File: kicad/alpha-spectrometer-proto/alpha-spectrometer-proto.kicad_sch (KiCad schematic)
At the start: 78 parts, among them J1 USB_B_Micro, J13 Anode, J14 Catode, J19 Conn, J2 Conn_01x01_Female, J20 Conn_01x01_Female, J21 Conn_01x01_Female, J22 Conn_01x01_Female, J3 Conn_01x01_Female, J4 BAT+, J5 BAT-, Q1 IRLML5203, SW1 SW_Push_SPDT, U1 MAX4477, U2 LM2733XMF, U3 MCP73831, U5 LMV7239, U6 MCP1700x, U7 LT3045xMSE, Y1 16

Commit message: удалено:       kicad/alpha-spectrometer-proto/alpha-spectrometer-proto-backups/alpha-spectrometer-proto-2024-11-04_113452.zip 	изменено:      kicad/alpha-spectrometer-proto/alpha-spectrometer-proto.kicad_pcb 	изменено:      kicad/alpha-spectrometer-proto/alpha-spectrometer-proto.kicad_prl 	изменено:      kicad/alpha-spectrometer-proto/alpha-spectrometer-proto.kicad_sch
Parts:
- L1: footprint Inductor_SMD:L_1206_3216Metric -> Inductor_SMD:L_1206_3216Metric_Pad1.42x1.75mm_HandSolder
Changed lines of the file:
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@@
     (property "Reference" "L1" (id 0) (at 57.15 19.9222 90))
     (property "Value" "22uH" (id 1) (at 57.15 22.4591 90))
-    (property "Footprint" "Inductor_SMD:L_1206_3216Metric" (id 2) (at 57.15 24.13 0)
+    (property "Footprint" "Inductor_SMD:L_1206_3216Metric_Pad1.42x1.75mm_HandSolder" (id 2) (at 57.15 24.13 0)
       (effects (font (size 1.27 1.27)) hide)
     )
@@
     )
     (path "/4628a448-92c4-457c-880d-943885ef5179"
-      (reference "L1") (unit 1) (value "22uH") (footprint "Inductor_SMD:L_1206_3216Metric")
+      (reference "L1") (unit 1) (value "22uH") (footprint "Inductor_SMD:L_1206_3216Metric_Pad1.42x1.75mm_HandSolder")
     )
     (path "/97df9df7-c99e-461c-b527-69bb284319db"

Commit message: удалено:       Documents/mr107+-1.png 	удалено:       Documents/mr107+-10.png 	удалено:       Documents/mr107+-11.png 	удалено:       Documents/mr107+-12.png 	удалено:       Documents/mr107+-13.png 	удалено:       Documents/mr107+-14.png 	удалено:       Documents/mr107+-2.png 	удалено:       Documents/mr107+-3.png 	удалено:       Documents/mr107+-4.png 	удалено:       Documents/mr107+-5.png 	удалено:       Documents/mr107+-6.png 	удалено:       Documents/mr107+-7.png 	удалено:       Documents/mr107+-8.png 	удалено:       Documents/mr107+-9.png 	изменено:      GNUPlot/mainChart-1.gp 	изменено:      GNUPlot/mainChart-1.gp~ 	изменено:      STM32CubeIDE/TestController/.settings/language.settings.xml 	изменено:      STM32CubeIDE/TestController/Core/Src/main.c 	изменено:      STM32CubeIDE/TestController/Debug/Core/Src/main.o 	изменено:      STM32CubeIDE/TestController/Debug/TestController.elf 	изменено:      STM32CubeIDE/TestController/Debug/TestController.list 	изменено:      STM32CubeIDE/TestController/TestController.ioc 	удалено:       kicad/alpha-spectrometer-proto/alpha-spectrometer-proto-backups/alpha-spectrometer-proto-2024-10-29_185625.zip 	удалено:       kicad/alpha-spectrometer-proto/alpha-spectrometer-proto-backups/alpha-spectrometer-proto-2024-10-29_190534.zip 	удалено:       kicad/alpha-spectrometer-proto/alpha-spectrometer-proto-backups/alpha-spectrometer-proto-2024-10-30_170209.zip 	удалено:       kicad/alpha-spectrometer-proto/alpha-spectrometer-proto-backups/alpha-spectrometer-proto-2024-10-30_171711.zip 	удалено:       kicad/alpha-spectrometer-proto/alpha-spectrometer-proto-backups/alpha-spectrometer-proto-2024-10-30_184706.zip 	удалено:       kicad/alpha-spectrometer-proto/alpha-spectrometer-proto-backups/alpha-spectrometer-proto-2024-10-30_185305.zip 	удалено:       kicad/alpha-spectrometer-proto/alpha-spectrometer-proto-backups/alpha-spectrometer-proto-2024-10-30_190038.zip 	удалено:       kicad/alpha-spectrometer-proto/alpha-spectrometer-proto-backup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
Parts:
- removed C14: 10, Capacitor_SMD:C_0603_1608Metric, symbol Device:C
- removed C15: 100n, Capacitor_SMD:C_0603_1608Metric, symbol Device:C
- removed C17: 10u, Capacitor_SMD:C_0603_1608Metric, symbol Device:C
- removed D3: AD5245, Package_TO_SOT_SMD:SOT-23-8_Handsoldering, symbol Anemometer_200_G473-rescue:AD5245-My_Library-My_Library-Anemometer_200_G473-res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
- added R15: 10, Resistor_SMD:R_0603_1608Metric, symbol Device:R
- added U4: AD8605, Package_TO_SOT_SMD:TSOT-23-5, symbol Amplifier_Operational:AD8603
- C3: value 1n -> 100p
- C4: value 10n -> 100n
- C5: value 10 -> 4.7
- C6: value 100n -> 10u
- R1: value 10k -> 100k
- R18: value 100k -> 51k
- R2: value 10k -> 20k
- R5: value 10k -> 1k
- R6: value 5.1M -> 2M
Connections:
- net +3V3: now also C6.2, U4.5 (V+)
- net Analog: now also R15.1; no longer R6.2, U1.1
- net GND: now also C6.1, U4.2 (V-); no longer R18.1, R5.2
- net at R6.1, U1.2 (-): now also R5.2; no longer R5.1
- net at U1.3 (+): now also C4.2, R1.2, R2.1, U1.5 (+)
- net at C5.2, R3.2, U1.7: now also R5.1; no longer C6.1
- net at R18.2: now also R6.2, U1.1, U4.3 (+); no longer U5.3 (+)
- new net: R15.2, U4.1, U4.4 (-)
- new net: R18.1, U5.3 (+)
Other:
- moved on the sheet: C1, C2, C22, C3, C32, C4, C5, R1, R18, R2, R3, R5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

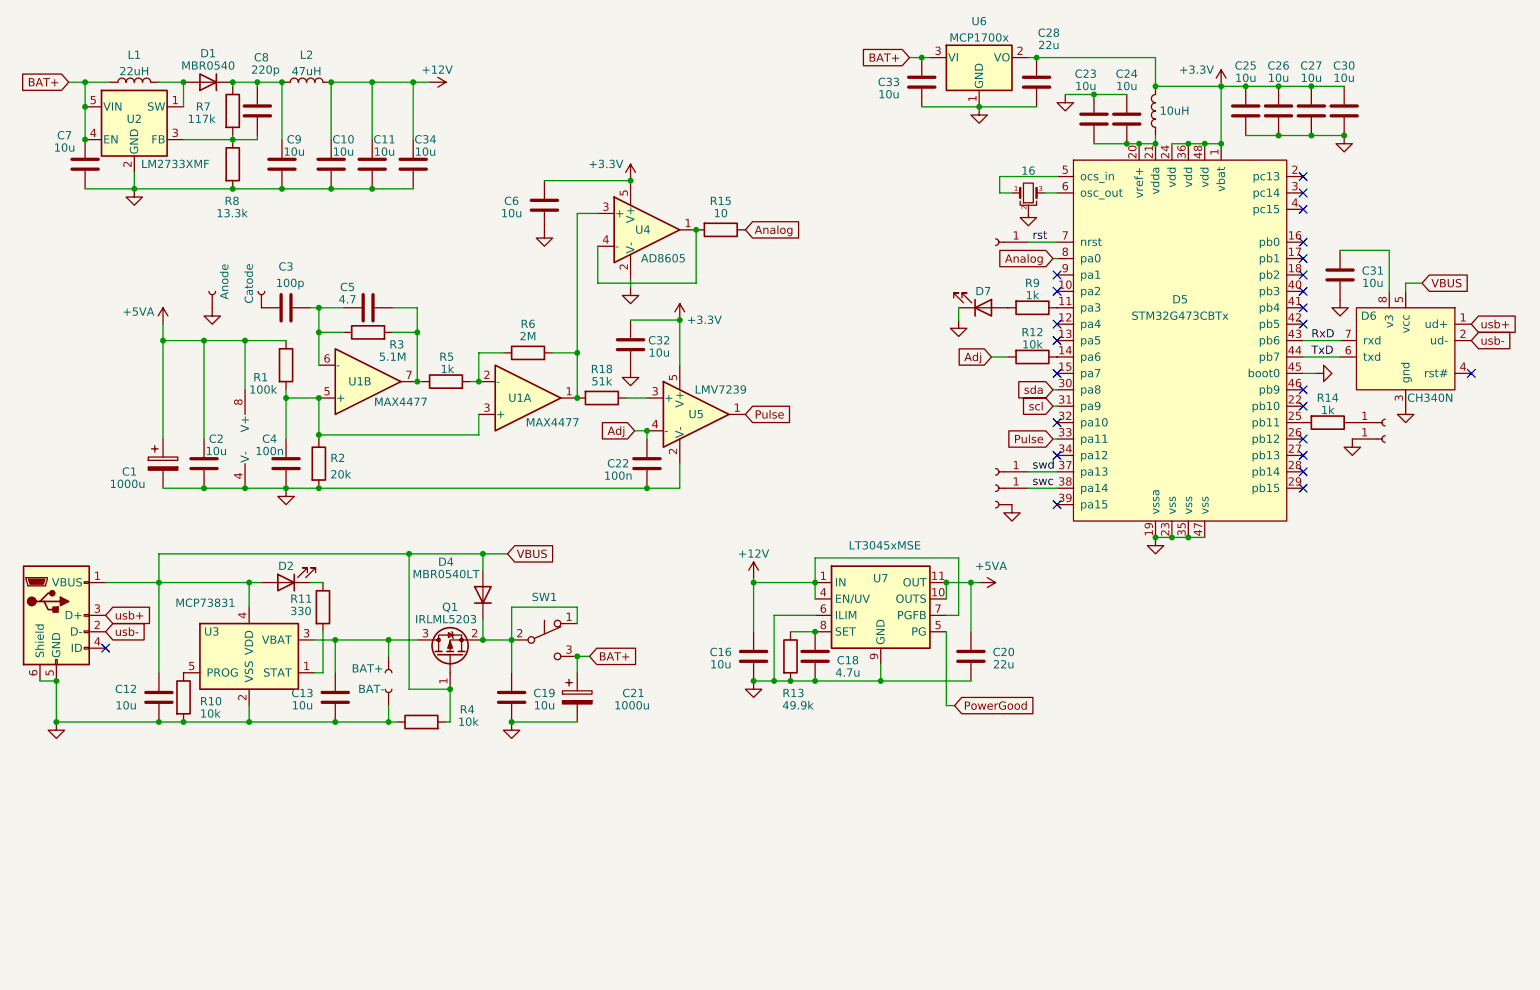
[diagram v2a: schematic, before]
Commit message: изменено:      STM32CubeIDE/TestController/.mxproject 	изменено:      STM32CubeIDE/TestController/.settings/language.settings.xml 	изменено:      STM32CubeIDE/TestController/Core/Inc/main.h 	изменено:      STM32CubeIDE/TestController/Core/Src/main.c 	изменено:      STM32CubeIDE/TestController/Core/Src/stm32g4xx_hal_msp.c 	изменено:      STM32CubeIDE/TestController/TestController.ioc 	удалено:       kicad/alpha-spectrometer-proto/alpha-spectrometer-proto-backups/alpha-spectrometer-proto-2024-10-31_190535.zip 	удалено:       kicad/alpha-spectrometer-proto/alpha-spectrometer-proto-backups/alpha-spectrometer-proto-2024-11-02_112209.zip 	удалено:       kicad/alpha-spectrometer-proto/alpha-spectrometer-proto-backups/alpha-spectrometer-proto-2024-11-03_173252.zip 	удалено:       kicad/alpha-spectrometer-proto/alpha-spectrometer-proto-backups/alpha-spectrometer-proto-2024-11-03_174252.zip 	удалено:       kicad/alpha-spectrometer-proto/alpha-spectrometer-proto-backups/alpha-spectrometer-proto-2024-11-03_175253.zip 	удалено:       kicad/alpha-spectrometer-proto/alpha-spectrometer-proto-backups/alpha-spectrometer-proto-2024-11-03_175855.zip 	удалено:       kicad/alpha-spectrometer-proto/alpha-spectrometer-proto-backups/alpha-spectrometer-proto-2024-11-03_201807.zip 	удалено:       kicad/alpha-spectrometer-proto/alpha-spectrometer-proto-backups/alpha-spectrometer-proto-2024-11-04_114242.zip 	удалено:       kicad/alpha-spectrometer-proto/alpha-spectrometer-proto-backups/alpha-spectrometer-proto-2024-11-04_115247.zip 	удалено:       kicad/alpha-spectrometer-proto/alpha-spectrometer-proto-backups/alpha-spectrometer-proto-2024-11-04_122306.zip 	изменено:      kicad/alpha-spectrometer-proto/alpha-spectrometer-proto.kicad_pcb 	изменено:      kicad/alpha-spectrometer-proto/alpha-spectrometer-proto.kicad_prl 	изменено:      kicad/alpha-spectrometer-proto/alpha-spectrometer-proto.kicad_pro 	изменено:      kicad/alpha-spectrometer-proto/alpha-spectrometer-proto.kicad_sch
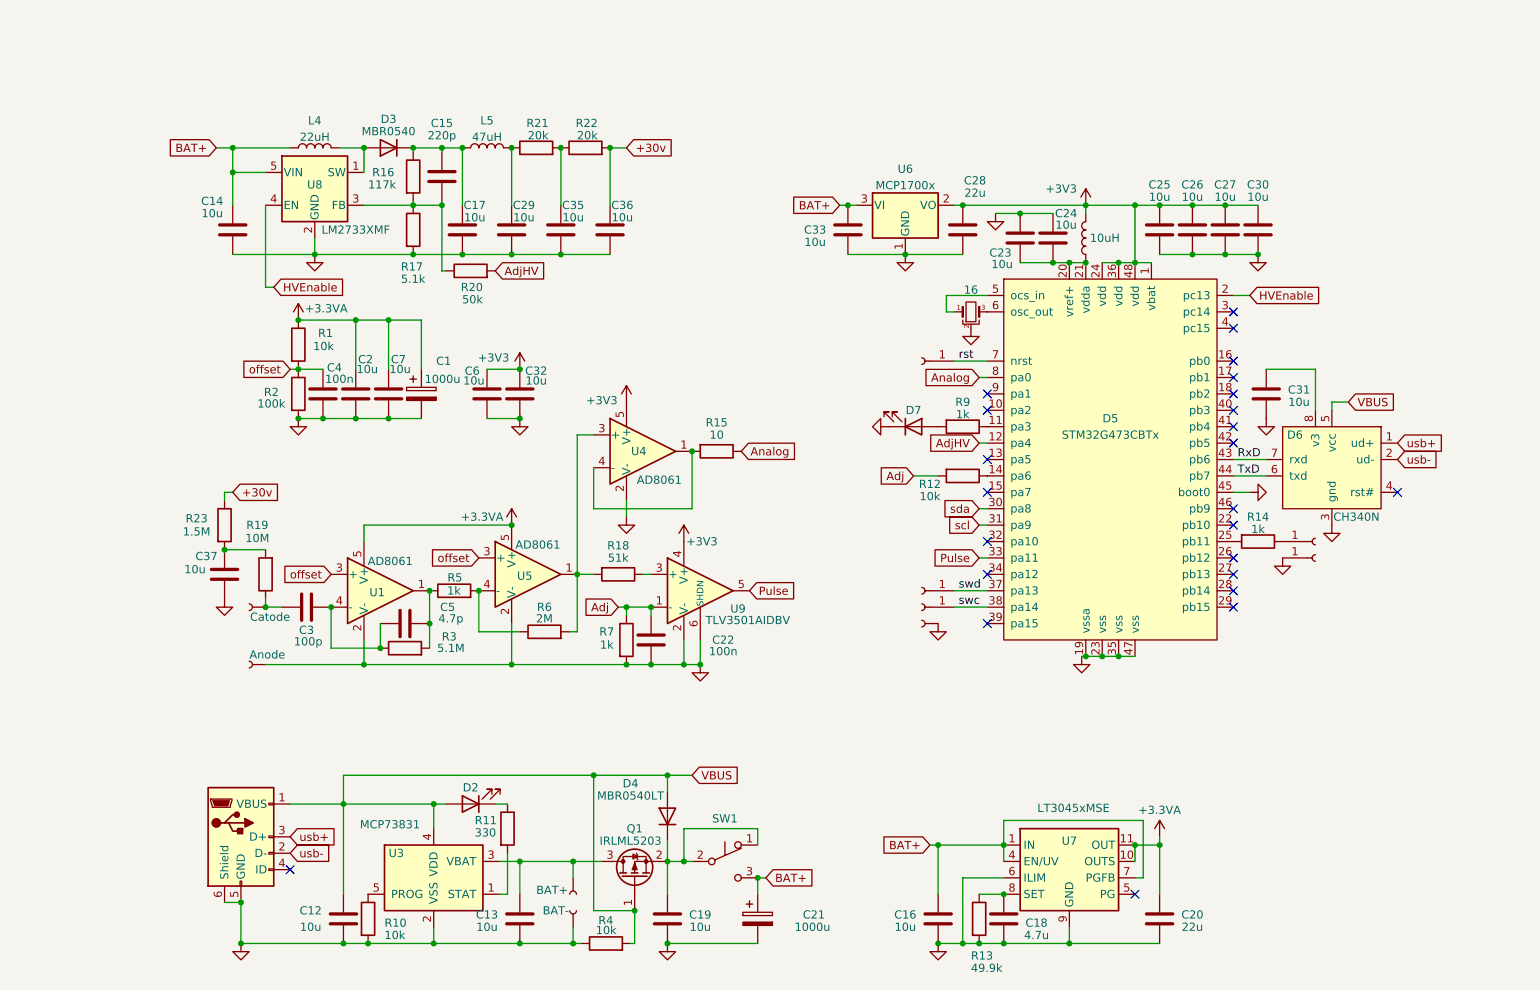
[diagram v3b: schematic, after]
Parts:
- removed C10, C11, C34, C9: 10u, Capacitor_SMD:C_0805_2012Metric, symbol Device:C
- removed C8: 220p, Capacitor_SMD:C_0603_1608Metric, symbol Device:C
- removed D1: MBR0540, Diode_SMD:D_SOD-123, symbol Device:D
- removed L1: 22uH, Inductor_SMD:L_1206_3216Metric_Pad1.42x1.75mm_HandSolder, symbol Device:L
- removed L2: 47uH, Inductor_SMD:L_0805_2012Metric, symbol Device:L
- removed R8: 13.3k, Resistor_SMD:R_0603_1608Metric, symbol Device:R
- removed U1: MAX4477, Package_SO:SSOP-8_2.95x2.8mm_P0.65mm, symbol Amplifier_Operational:AD8676xR
- removed U2: LM2733XMF, Package_TO_SOT_SMD:SOT-23-5, symbol Regulator_Switching:LM2733XMF
- removed U5: LMV7239, Package_TO_SOT_SMD:SOT-23-5, symbol Comparator:LMV7219M5
- added C14, C17, C29, C35, C36: 10u, Capacitor_SMD:C_0805_2012Metric, symbol Device:C
- added C15: 220p, Capacitor_SMD:C_0603_1608Metric, symbol Device:C
- added C37: 10u, Capacitor_SMD:C_0603_1608Metric, symbol Device:C
- added D3: MBR0540, Diode_SMD:D_SOD-123, symbol Device:D
- added L4: 22uH, Inductor_SMD:L_1206_3216Metric_Pad1.42x1.75mm_HandSolder, symbol Device:L
- added L5: 47uH, Inductor_SMD:L_0805_2012Metric, symbol Device:L
- added R16: 117k, Resistor_SMD:R_0603_1608Metric, symbol Device:R
- added R17: 5.1k, Resistor_SMD:R_0603_1608Metric, symbol Device:R
- added R19: 10M, Resistor_SMD:R_0603_1608Metric, symbol Device:R
- added R20: 50k, Resistor_SMD:R_0603_1608Metric, symbol Device:R
- added R21, R22: 20k, Resistor_SMD:R_0603_1608Metric, symbol Device:R
- added R23: 1.5M, Resistor_SMD:R_0603_1608Metric, symbol Device:R
- added U1, U5: AD8061, Package_TO_SOT_SMD:TSOT-23-5, symbol Amplifier_Operational:AD8603
- added U8: LM2733XMF, Package_TO_SOT_SMD:SOT-23-5, symbol Regulator_Switching:LM2733XMF
- added U9: TLV3501AIDBV, Package_TO_SOT_SMD:SOT-23-6, symbol Comparator:TLV3501AIDBV
- C5: value 4.7 -> 4.7p
- C7: footprint Capacitor_SMD:C_0805_2012Metric -> Capacitor_SMD:C_0603_1608Metric
- R1: value 100k -> 10k
- R2: value 20k -> 100k
- R7: value 117k -> 1k
- U4: value AD8605 -> AD8061
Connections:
- net +12V is gone; now on net BAT+: C16.2, U7.1 (IN), U7.2 (IN), U7.3 (IN), U7.4 (EN/UV), U7.7 (PGFB)
- net +3V3: now also U9.4 (V+)
- net Adj: now also R7.1, U9.1 (-)
- net BAT+: now also C14.2, L4.1, U8.5 (VIN); no longer C7.2
- net GND: now also R7.2, C14.1, C17.1, C29.1, C35.1, C36.1, C37.1, R17.2, U1.2 (V-), U5.2 (V-), U8.2 (GND), U9.2 (V-), U9.6 (SHDN)
- net Pulse: now also U9.5
- net at R5.2, R6.1: now also U5.4 (-)
- net at R18.2, R6.2, U4.3 (+): now also U5.1
- net at C3.2, C5.1, R3.1: now also U1.4 (-)
- net at C5.2, R3.2, R5.1: now also U1.1
- net at R18.1: now also U9.3 (+)
- net at C3.1, J14.1: now also R19.1
- net offset: now reaches C4.2, R1.2, R2.1
- net offset: now also U1.3 (+), U5.3 (+)
- net AdjHV: now reaches D5.12 (pa4)
- net AdjHV: now also R20.2
- net HVEnable: now reaches D5.2 (pc13)
- net HVEnable: now also U8.4 (EN)
- net +5VA renamed +3.3VA
- net +3.3VA: now also C7.2, U1.5 (V+), U5.5 (V+)
- net PowerGood: no longer names the net of U7.5 (PG)
- new net: C15.2, C17.2, D3.1 (K), L5.1, R16.1
- new net: C15.1, R16.2, R17.1, R20.1, U8.3 (FB)
- new net: C29.2, L5.2, R21.1
- new net: C35.2, R21.2, R22.1
- new net: D3.2 (A), L4.2, U8.1 (SW)
- new net: C37.2, R19.2, R23.2
- new net +30v: C36.2, R22.2, R23.1
- no-connect marks 25 -> 24
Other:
- moved on the sheet: C1, C12, C13, C16, C18, C19, C2, C20, C21, C22, C23, C24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

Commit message: изменено:      STM32CubeIDE/TestController/.mxproject 	изменено:      STM32CubeIDE/TestController/.settings/language.settings.xml 	изменено:      STM32CubeIDE/TestController/Core/Src/main.c 	изменено:      STM32CubeIDE/TestController/Debug/Core/Src/AD5245.o 	изменено:      STM32CubeIDE/TestController/Debug/Core/Src/main.cyclo 	изменено:      STM32CubeIDE/TestController/Debug/Core/Src/main.o 	изменено:      STM32CubeIDE/TestController/Debug/Core/Src/main.su 	изменено:      STM32CubeIDE/TestController/Debug/Core/Src/stm32g4xx_hal_msp.cyclo 	изменено:      STM32CubeIDE/TestController/Debug/Core/Src/stm32g4xx_hal_msp.o 	изменено:      STM32CubeIDE/TestController/Debug/Core/Src/stm32g4xx_hal_msp.su 	изменено:      STM32CubeIDE/TestController/Debug/Core/Src/stm32g4xx_it.o 	изменено:      STM32CubeIDE/TestController/Debug/Core/Src/system_stm32g4xx.o 	изменено:      STM32CubeIDE/TestController/Debug/Drivers/STM32G4xx_HAL_Driver/Src/stm32g4xx_hal.o 	изменено:      STM32CubeIDE/TestController/Debug/Drivers/STM32G4xx_HAL_Driver/Src/stm32g4xx_hal_adc.o 	изменено:      STM32CubeIDE/TestController/Debug/Drivers/STM32G4xx_HAL_Driver/Src/stm32g4xx_hal_adc_ex.o 	изменено:      STM32CubeIDE/TestController/Debug/Drivers/STM32G4xx_HAL_Driver/Src/stm32g4xx_hal_cortex.o 	изменено:      STM32CubeIDE/TestController/Debug/Drivers/STM32G4xx_HAL_Driver/Src/stm32g4xx_hal_dac.o 	изменено:      STM32CubeIDE/TestController/Debug/Drivers/STM32G4xx_HAL_Driver/Src/stm32g4xx_hal_dac_ex.o 	изменено:      STM32CubeIDE/TestController/Debug/Drivers/STM32G4xx_HAL_Driver/Src/stm32g4xx_hal_dma.o 	изменено:      STM32CubeIDE/TestController/Debug/Drivers/STM32G4xx_HAL_Driver/Src/stm32g4xx_hal_dma_ex.o 	изменено:      STM32CubeIDE/TestController/Debug/Drivers/STM32G4xx_HAL_Driver/Src/stm32g4xx_hal_exti.o 	изменено:      STM32CubeIDE/TestController/Debug/Drivers/STM32G4xx_HAL_Driver/Src/stm32g4xx_hal_flash.o 	изменено:      STM32CubeIDE/TestController/Debug/Drivers/STM32G4xx_HAL_Driver/Src/stm32g4xx_hal_flash_e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
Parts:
- added C8: 4.7p, Capacitor_SMD:C_0603_1608Metric, symbol Device:C
- R13: value 49.9k -> 33.2k
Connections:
- net at R5.2, R6.1, U5.4 (-): now also C8.1
- net at R18.2, R6.2, U4.3 (+)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: now also C8.2
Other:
- moved on the sheet: R6
